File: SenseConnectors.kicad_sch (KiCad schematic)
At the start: 1 part, among them J12 SenseConn1

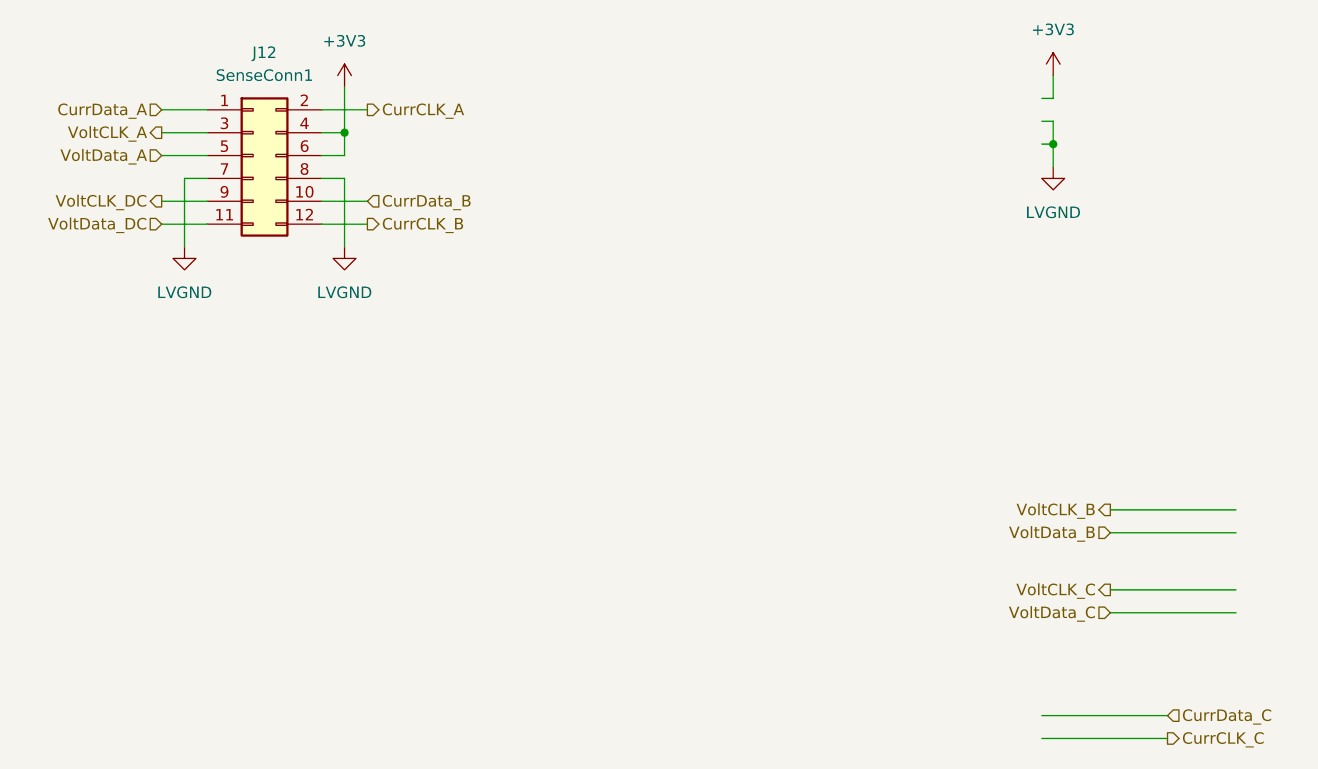
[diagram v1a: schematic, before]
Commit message: bulk caps sheet + adc data clk trace crosstalk
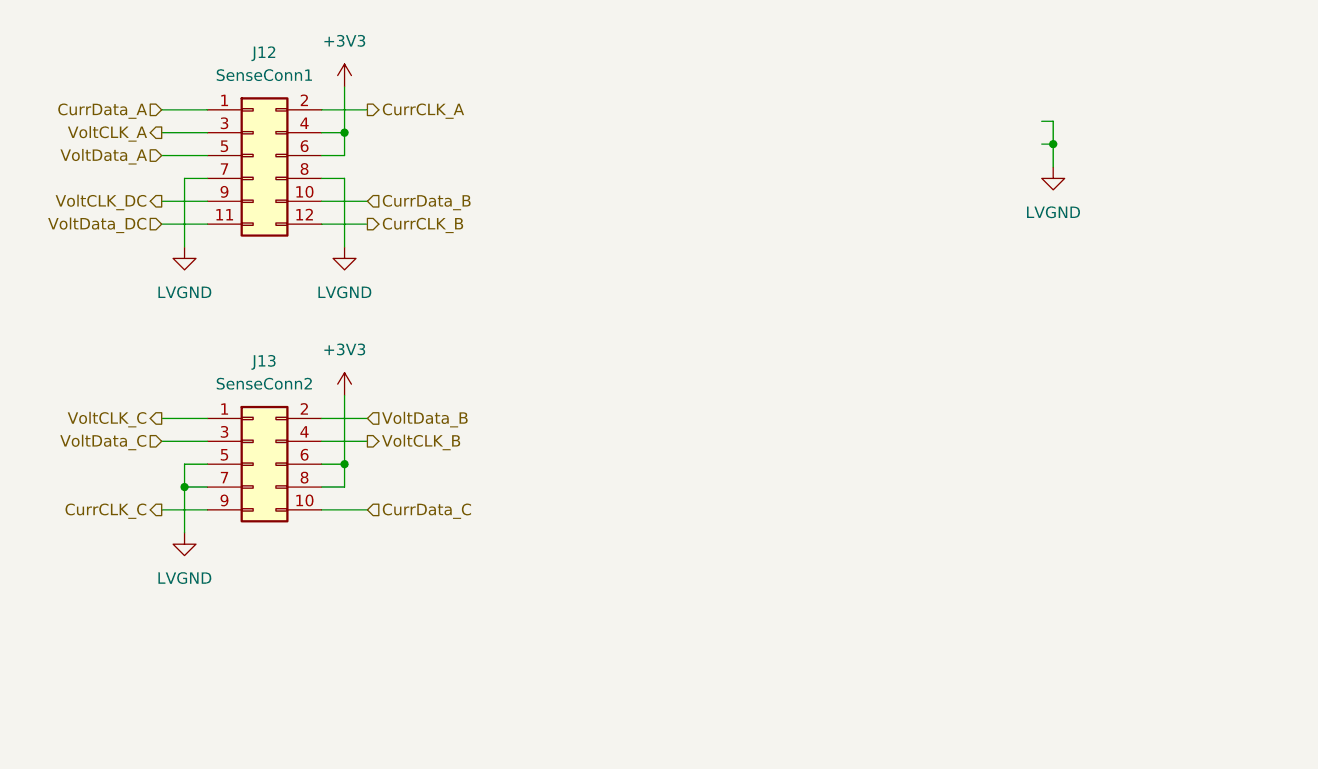
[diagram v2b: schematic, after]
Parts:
- added J13: SenseConn2, Connector_PinHeader_2.54mm:PinHeader_2x05_P2.54mm_Vertical, symbol Connector_Generic:Conn_02x05_Odd_Even
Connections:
- net +3V3: now also J13.6 (Pin_6), J13.8 (Pin_8)
- net CurrCLK_C: now also J13.9 (Pin_9)
- net CurrData_C: now also J13.10 (Pin_10)
- net LVGND: now also J13.5 (Pin_5), J13.7 (Pin_7)
- net VoltCLK_B: now also J13.4 (Pin_4)
- net VoltCLK_C: now also J13.1 (Pin_1)
- net VoltData_B: now also J13.2 (Pin_2)
- net VoltData_C: now also J13.3 (Pin_3)

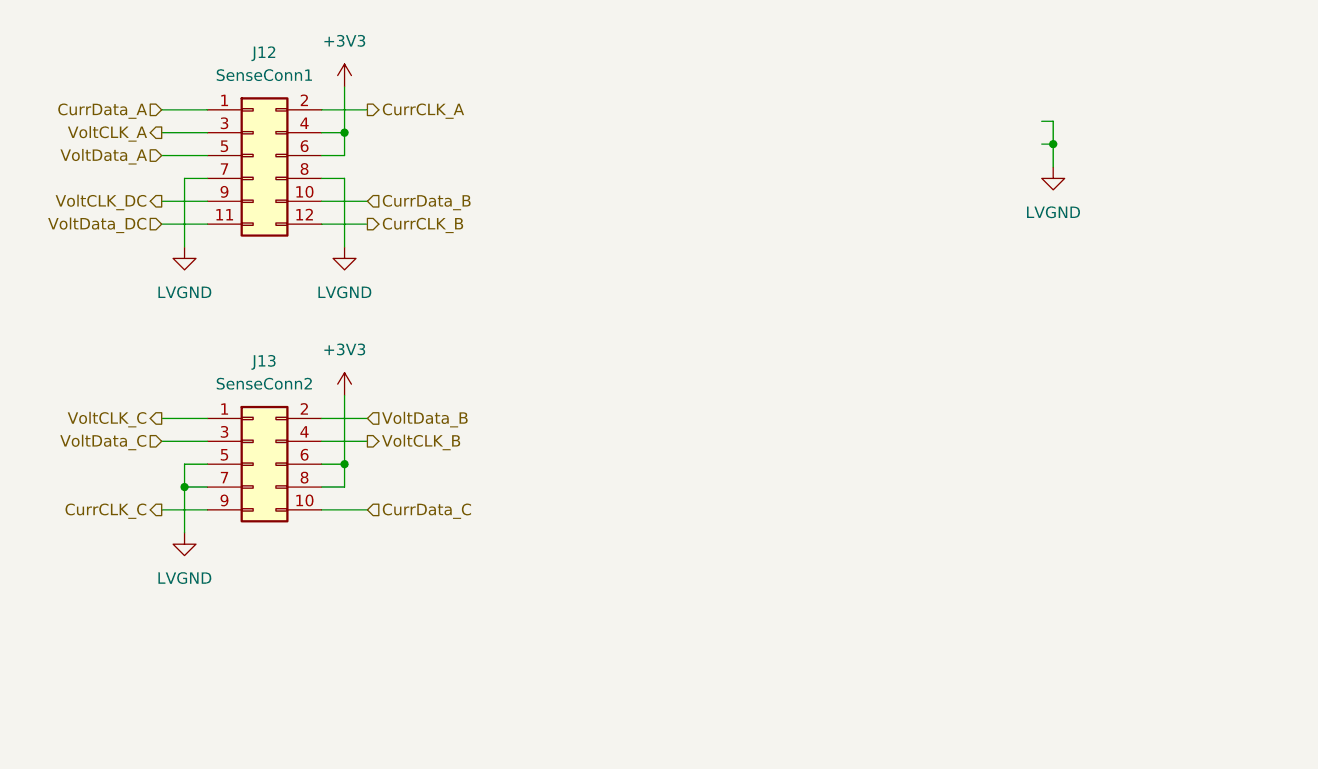
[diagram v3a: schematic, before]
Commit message: gate driver connector 1 layout and isodcdc L
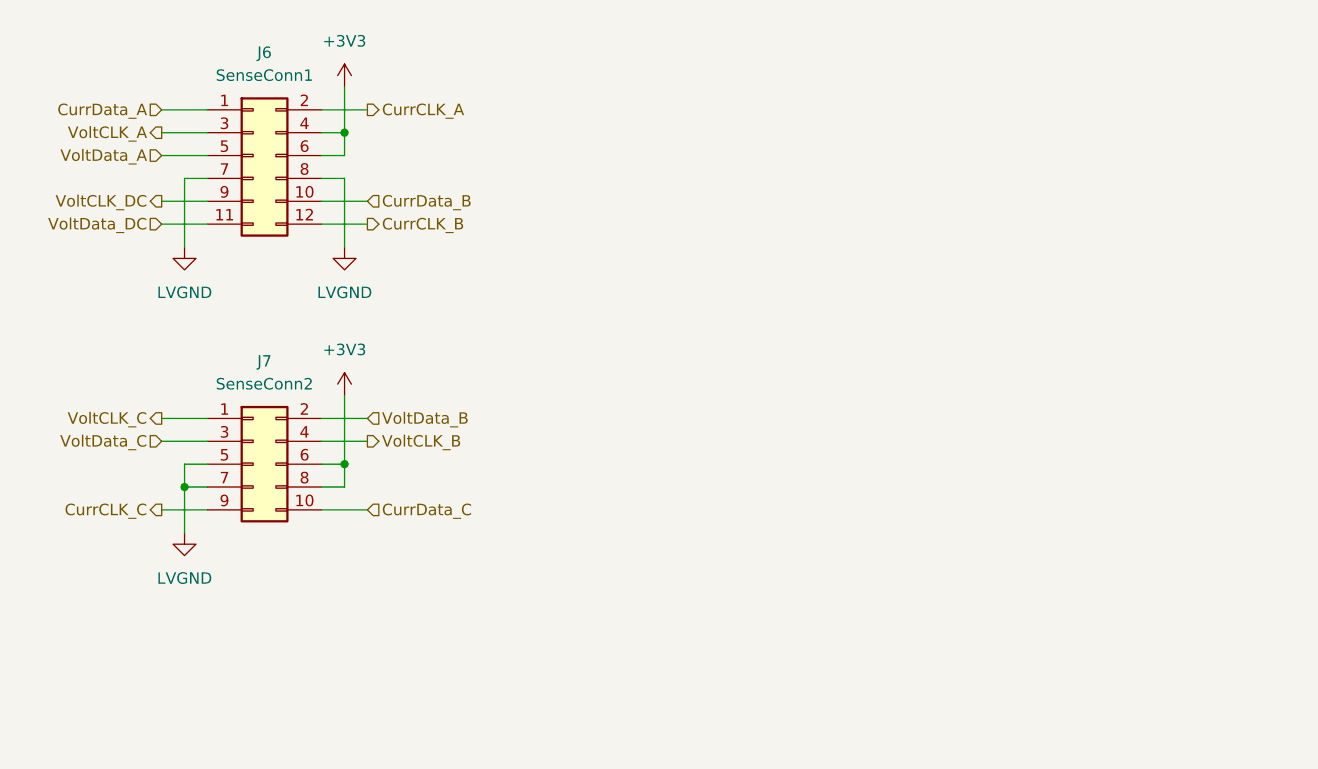
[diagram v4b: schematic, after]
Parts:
- renumbered J12 to J6, J13 to J7
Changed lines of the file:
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@@
-	)
-	(junction
-		(at 187.96 59.69)
-		(diameter 0)
-		(color 0 0 0 0)
 	)
 	(junction
@@
 	(wire
 		(pts
-			(xy 187.96 59.69) (xy 186.69 59.69)
-		)
-		(stroke
-			(width 0)
-			(type default)
-		)
-	)
-	(wire
-		(pts
 			(xy 93.98 60.96) (xy 88.9 60.96)
 		)
@@
 	(wire
 		(pts
-			(xy 187.96 59.69) (xy 187.96 57.15)
-		)
-		(stroke
-			(width 0)
-			(type default)
-		)
-	)
-	(wire
-		(pts
 			(xy 91.44 63.5) (xy 91.44 71.12)
 		)
@@
 	(wire
 		(pts
-			(xy 187.96 57.15) (xy 186.69 57.15)
-		)
-		(stroke
-			(width 0)
-			(type default)
-		)
-	)
-	(wire
-		(pts
 			(xy 106.68 90.17) (xy 111.76 90.17)
 		)
@@
 		(pts
 			(xy 93.98 55.88) (xy 88.9 55.88)
-		)
-		(stroke
-			(width 0)
-			(type default)
-		)
-	)
-	(wire
-		(pts
-			(xy 187.96 62.23) (xy 187.96 59.69)
 		)
 		(stroke
@@
 		(dnp no)
 		(fields_autoplaced yes)
-		(property "Reference" "#PWR0262"
+		(property "Reference" "#PWR0232"
 			(at 109.22 77.47 0)
 			(effects
@@
 			(project "TractionInverter"
 				(path "/bc91ffbf-afc6-42bb-9d28-6a3fecc21fcc/3aaba1fa-a0df-4eca-b815-30424e38ce2f"
-					(reference "#PWR0262")
+					(reference "#PWR0232")
 					(unit 1)
 				)
@@
 		(dnp no)
 		(fields_autoplaced yes)
-		(property "Reference" "#PWR0261"
+		(property "Reference" "#PWR0231"
 			(at 91.44 77.47 0)
 			(effects
@@
 			(project "TractionInverter"
 				(path "/bc91ffbf-afc6-42bb-9d28-6a3fecc21fcc/3aaba1fa-a0df-4eca-b815-30424e38ce2f"
-					(reference "#PWR0261")
+					(reference "#PWR0231")
 					(unit 1)
 				)
@@
 		(dnp no)
 		(fields_autoplaced yes)
-		(property "Reference" "J13"
+		(property "Reference" "J7"
 			(at 100.33 83.82 0)
 			(effects
@@
 			(project ""
 				(path "/bc91ffbf-afc6-42bb-9d28-6a3fecc21fcc/3aaba1fa-a0df-4eca-b815-30424e38ce2f"
-					(reference "J13")
+					(reference "J7")
 					(unit 1)
 				)
@@
 		(dnp no)
 		(fields_autoplaced yes)
-		(property "Reference" "#PWR0259"
+		(property "Reference" "#PWR0229"
 			(at 109.22 57.15 0)
 			(effects
@@
 			(project "TractionInverter"
 				(path "/bc91ffbf-afc6-42bb-9d28-6a3fecc21fcc/3aaba1fa-a0df-4eca-b815-30424e38ce2f"
-					(reference "#PWR0259")
+					(reference "#PWR0229")
 					(unit 1)
 				)
@@
 		(dnp no)
 		(fields_autoplaced yes)
-		(property "Reference" "#PWR0263"
+		(property "Reference" "#PWR0233"
 			(at 109.22 91.44 0)
 			(effects
@@
 			(project "TractionInverter"
 				(path "/bc91ffbf-afc6-42bb-9d28-6a3fecc21fcc/3aaba1fa-a0df-4eca-b815-30424e38ce2f"
-					(reference "#PWR0263")
+					(reference "#PWR0233")
 					(unit 1)
 				)
@@
 		(dnp no)
 		(fields_autoplaced yes)
-		(property "Reference" "#PWR0264"
+		(property "Reference" "#PWR0234"
 			(at 91.44 109.22 0)
 			(effects
@@
 			(project "TractionInverter"
 				(path "/bc91ffbf-afc6-42bb-9d28-6a3fecc21fcc/3aaba1fa-a0df-4eca-b815-30424e38ce2f"
-					(reference "#PWR0264")
+					(reference "#PWR0234")
 					(unit 1)
 				)
@@
 		(dnp no)
 		(fields_autoplaced yes)
-		(property "Reference" "J12"
+		(property "Reference" "J6"
 			(at 100.33 49.53 0)
 			(effects
@@
 			(project "TractionInverter"
 				(path "/bc91ffbf-afc6-42bb-9d28-6a3fecc21fcc/3aaba1fa-a0df-4eca-b815-30424e38ce2f"
-					(reference "J12")
+					(reference "J6")
 					(unit 1)
 				)
-			)
-		)
-	)
-	(symbol
-		(lib_id "power:GND")
-		(at 187.96 62.23 0)
-		(mirror y)
-		(unit 1)
-		(exclude_from_sim no)
-		(in_bom yes)
-		(on_board yes)
-		(dnp no)
-		(fields_autoplaced yes)
-		(property "Reference" "#PWR0260"
-			(at 187.96 68.58 0)
-			(effects
-				(font
-					(size 1.27 1.27)
-				)
-				(hide yes)
-			)
-		)
-		(property "Value" "LVGND"
-			(at 187.96 67.31 0)
-			(effects
-				(font
-					(size 1.27 1.27)
-				)
-			)
-		)
-		(property "Footprint" ""
-			(at 187.96 62.23 0)
-			(effects
-				(font
-					(size 1.27 1.27)
-				)
-				(hide yes)
-			)
-		)
-		(property "Datasheet" ""
-			(at 187.96 62.23 0)
-			(effects
-				(font
-					(size 1.27 1.27)
-				)
-				(hide yes)
-			)
-		)
-		(property "Description" "Power symbol creates a global label with name \"GND\" , ground"
-			(at 187.96 62.23 0)
-			(effects
-				(font
-					(size 1.27 1.27)
-				)
-				(hide yes)
-			)
-		)
-		(pin "1"
-		)
-		(instances
-			(project "TractionInverter"
-				(path "/bc91ffbf-afc6-42bb-9d28-6a3fecc21fcc/3aaba1fa-a0df-4eca-b815-30424e38ce2f"
-					(reference "#PWR0260")
-					(unit 1)
-				)
